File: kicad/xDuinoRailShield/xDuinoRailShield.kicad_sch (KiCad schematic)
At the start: 36 parts, among them J5 Screw_Terminal_01x02, Q2 S8050, Q3 S8550, Q4 S8050, Q5 S8550, U1 TPS5430DDA, U2 6N137, U3 EL817

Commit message: Heavy refactoring
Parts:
- removed C1, C4, C5: 10uF, Capacitor_SMD:C_1206_3216Metric, symbol Device:C
- removed C2: 10nF, Capacitor_SMD:C_0805_2012Metric, symbol Device:C
- removed C3: 10uF, Capacitor_SMD:CP_Elec_6.3x3.9, symbol Device:C_Polarized
- removed C6: 1nF, Capacitor_SMD:C_0805_2012Metric, symbol Device:C
- removed D2, D6, D7, D8: D, Diode_SMD:D_SMA, symbol Device:D
- removed D4: D_Schottky, Diode_SMD:D_SMC, symbol Device:D_Schottky
- removed D5: 1N4148W, Diode_SMD:D_SOD-123, symbol Diode:1N4148W
- removed JP_RAILCOM1: SolderJumper_2_Open, Jumper:SolderJumper-2_P1.3mm_Open_TrianglePad1.0x1.5mm, symbol Jumper:SolderJumper_2_Open
- removed L1: 22uH, Inductor_SMD:L_12x12mm_H8mm, symbol Device:L
- removed Q2, Q4: S8050, Package_TO_SOT_SMD:SOT-23, symbol Transistor_BJT:S8050
- removed Q3, Q5: S8550, Package_TO_SOT_SMD:SOT-23, symbol Transistor_BJT:S8550
- removed R10: 220R, Resistor_SMD:R_0805_2012Metric_Pad1.20x1.40mm_HandSolder, symbol Device:R
- removed R11: 5k, Resistor_SMD:R_0805_2012Metric_Pad1.20x1.40mm_HandSolder, symbol Device:R
- removed R3, R7: 10k, Resistor_SMD:R_0805_2012Metric_Pad1.20x1.40mm_HandSolder, symbol Device:R
- removed R5: 1.58k, Resistor_SMD:R_0805_2012Metric_Pad1.20x1.40mm_HandSolder, symbol Device:R
- removed R5: 22k, Resistor_SMD:R_0805_2012Metric_Pad1.20x1.40mm_HandSolder, symbol Device:R
- removed R6: 1k3, Resistor_SMD:R_0805_2012Metric_Pad1.20x1.40mm_HandSolder, symbol Device:R
- removed R8: 22, Resistor_SMD:R_0805_2012Metric_Pad1.20x1.40mm_HandSolder, symbol Device:R
- removed R9: 6k8, Resistor_SMD:R_0805_2012Metric_Pad1.20x1.40mm_HandSolder, symbol Device:R
- removed U1: TPS5430DDA, Package_SO:TI_SO-PowerPAD-8_ThermalVias, symbol Regulator_Switching:TPS5430DDA
- removed U2: 6N137, Package_DIP:DIP-8_W7.62mm, symbol Isolator:6N137
- removed U3: EL817, Package_DIP:DIP-4_W7.62mm_SMDSocket_SmallPads, symbol Isolator:EL817
- D1, D3: LCSC (none) -> C2297
- R1, R2: LCSC (none) -> C26010
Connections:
- net DCC_MM: now also A1.17 (D2); no longer A1.18 (D3)
- net RAILCOM_DATA: now also A1.18 (D3); no longer A1.17 (D2)
- no-connect marks 26 -> 24
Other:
- added sheet AC-DC buck convertor (ad-dc-buck-convertor.kicad_sch)
- added sheet Digital Signal Extraction (digital-signal-extraction.kicad_sch)
- added sheet Railcom-Feedback (railcom-feedback.kicad_sch)
- moved on the sheet: A1, D1, D3, J5, R1, R2

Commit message: Shield extracted
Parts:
- removed A1: Arduino_UNO_R3, Olis_Footprints:Arduino_UNO_R3_Double_Rows, symbol MCU_Module:Arduino_UNO_R3
- removed D1, D3: LED, LED_SMD:LED_0805_2012Metric_Pad1.15x1.40mm_HandSolder, symbol Device:LED
- removed J5: Screw_Terminal_01x02, TerminalBlock_4Ucon:TerminalBlock_4Ucon_1x02_P3.50mm_Vertical, symbol Connector:Screw_Terminal_01x02
- removed R1, R2: 3k3, Resistor_SMD:R_0805_2012Metric_Pad1.20x1.40mm_HandSolder, symbol Device:R
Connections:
- no-connect marks 24 -> 1
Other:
- added sheet IO Carrier Board (io-carrier-board.kicad_sch)

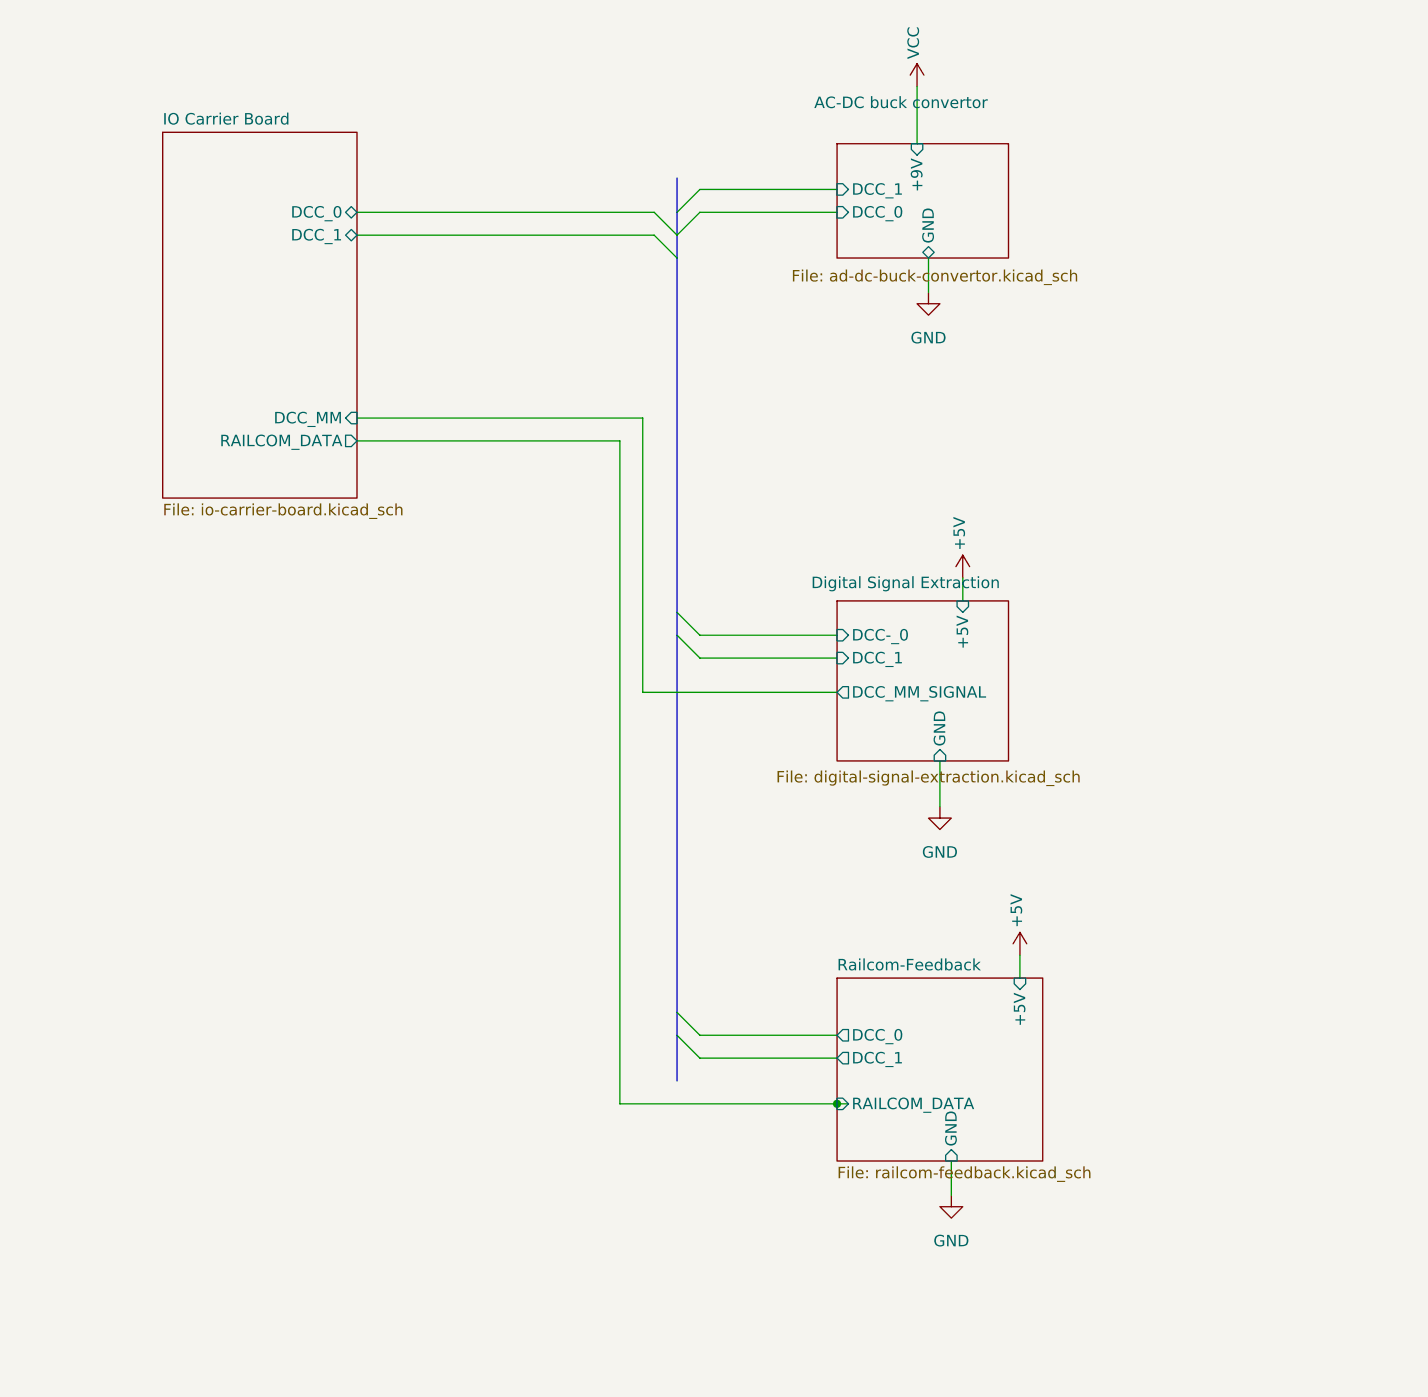
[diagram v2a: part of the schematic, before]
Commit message: Add more extractor
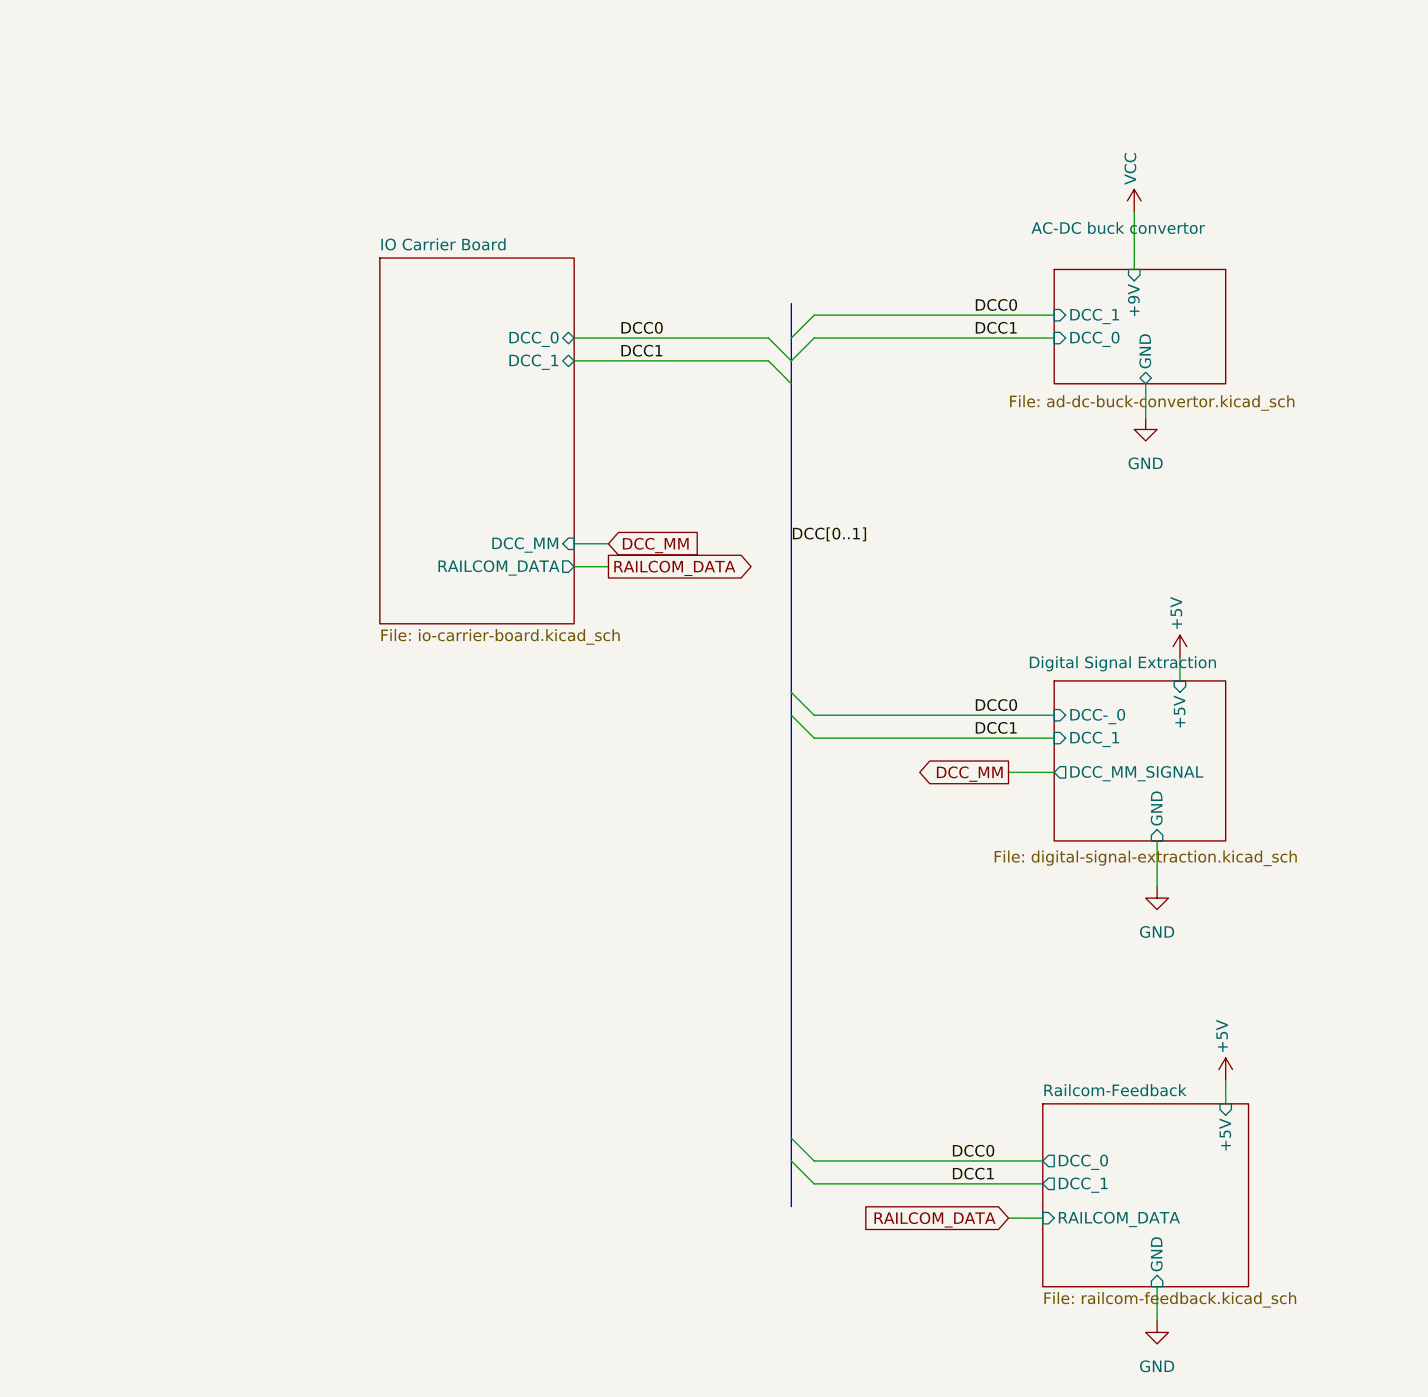
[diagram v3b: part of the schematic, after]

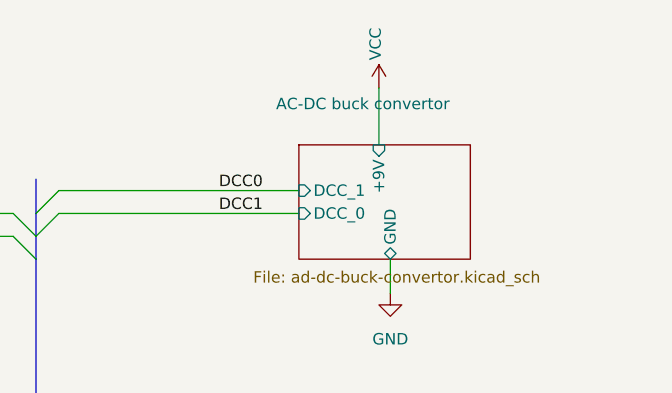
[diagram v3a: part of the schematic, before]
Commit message: More options, more Partnumbers
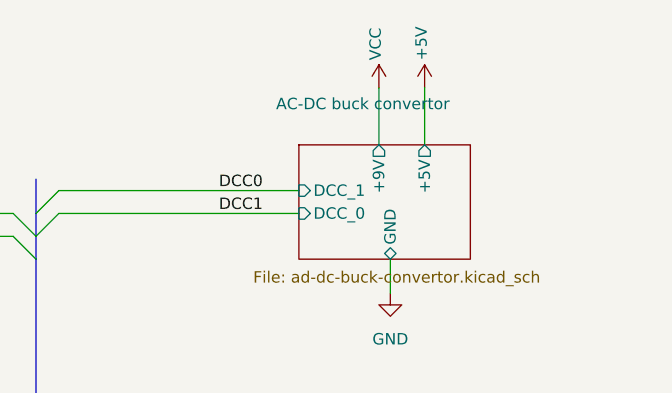
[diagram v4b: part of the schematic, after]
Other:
- sheet AC-DC buck convertor ports: added +5V; removed none
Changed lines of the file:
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@@
+    (stroke (width 0) (type default))
+  )
+  (wire (pts (xy 147.32 40.64) (xy 147.32 46.99))
     (stroke (width 0) (type default))
   )
@@
     )
   )
+  (symbol (lib_id "power:+5V") (at 147.32 40.64 0) (mirror y) (unit 1)
+    (in_bom yes) (on_board yes) (dnp no)
+    (property "Reference" "#PWR0107" (at 147.32 44.45 0)
+      (effects (font (size 1.27 1.27)) hide)
+    )
+    (property "Value" "+5V" (at 146.9644 37.592 90)
+      (effects (font (size 1.27 1.27)) (justify left))
+    )
+    (property "Footprint" "" (at 147.32 40.64 0)
+      (effects (font (size 1.27 1.27)))
+    )
+    (property "Datasheet" "" (at 147.32 40.64 0)
+      (effects (font (size 1.27 1.27)))
+    )
+    (pin "1")
+    (instances
+      (project "xDuinoRailShield"
+        (path "/e63e39d7-6ac0-4ffd-8aa3-1841a4541b55"
+          (reference "#PWR0107") (unit 1)
+        )
+      )
+    )
+  )
   (symbol (lib_id "power:VCC") (at 142.24 40.64 0) (mirror y) (unit 1)
     (in_bom yes) (on_board yes) (dnp no)
-    (property "Reference" "#PWR010" (at 142.24 44.45 0)
+    (property "Reference" "#PWR0101" (at 142.24 44.45 0)
       (effects (font (size 1.27 1.27)) hide)
     )
@@
       (project "xDuinoRailShield"
         (path "/e63e39d7-6ac0-4ffd-8aa3-1841a4541b55"
-          (reference "#PWR010") (unit 1)
+          (reference "#PWR0101") (unit 1)
         )
       )
@@
       (project "xDuinoRailShield"
         (path "/e63e39d7-6ac0-4ffd-8aa3-1841a4541b55"
-          (reference "#PWR014") (unit 1)
+          (reference "#PWR0103") (unit 1)
         )
       )
@@
       (project "xDuinoRailShield"
         (path "/e63e39d7-6ac0-4ffd-8aa3-1841a4541b55"
-          (reference "#PWR013") (unit 1)
+          (reference "#PWR0102") (unit 1)
         )
       )
@@
   (symbol (lib_id "power:+5V") (at 152.4 137.16 0) (mirror y) (unit 1)
     (in_bom yes) (on_board yes) (dnp no)
-    (property "Reference" "#PWR017" (at 152.4 140.97 0)
+    (property "Reference" "#PWR0106" (at 152.4 140.97 0)
       (effects (font (size 1.27 1.27)) hide)
     )
@@
       (project "xDuinoRailShield"
         (path "/e63e39d7-6ac0-4ffd-8aa3-1841a4541b55"
-          (reference "#PWR017") (unit 1)
+          (reference "#PWR0106") (unit 1)
         )
       )
@@
   (symbol (lib_id "power:+5V") (at 147.32 90.17 0) (mirror y) (unit 1)
     (in_bom yes) (on_board yes) (dnp no)
-    (property "Reference" "#PWR015" (at 147.32 93.98 0)
+    (property "Reference" "#PWR0105" (at 147.32 93.98 0)
       (effects (font (size 1.27 1.27)) hide)
     )
@@
       (project "xDuinoRailShield"
         (path "/e63e39d7-6ac0-4ffd-8aa3-1841a4541b55"
-          (reference "#PWR015") (unit 1)
+          (reference "#PWR0105") (unit 1)
         )
       )
@@
       (project "xDuinoRailShield"
         (path "/e63e39d7-6ac0-4ffd-8aa3-1841a4541b55"
-          (reference "#PWR016") (unit 1)
+          (reference "#PWR0104") (unit 1)
         )
       )
@@
       (effects (font (size 1.27 1.27)) (justify left))
     )
-    (pin "+9V" input (at 142.24 46.99 90)
+    (pin "+9V" output (at 142.24 46.99 90)
       (effects (font (size 1.27 1.27)) (justify right))
     )
@@
       (effects (font (size 1.27 1.27)) (justify left))
     )
-    (instances
+    (pin "+5V" output (at 147.32 46.99 90)
+      (effects (font (size 1.27 1.27)) (justify right))
+    )
+    (instances

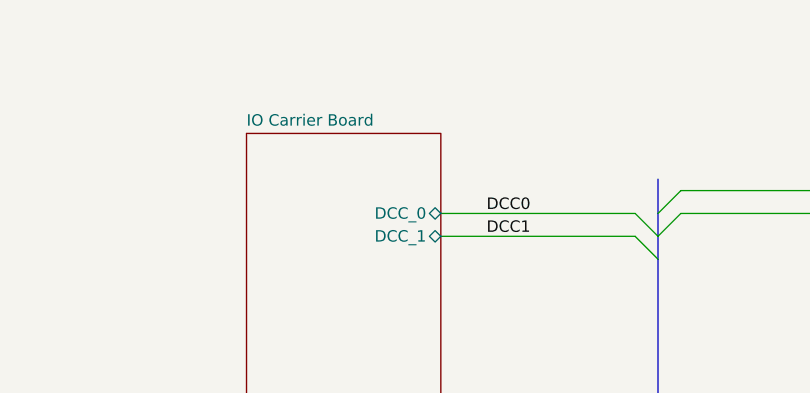
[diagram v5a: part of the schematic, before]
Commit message: Power Rails added to Arduino IO board
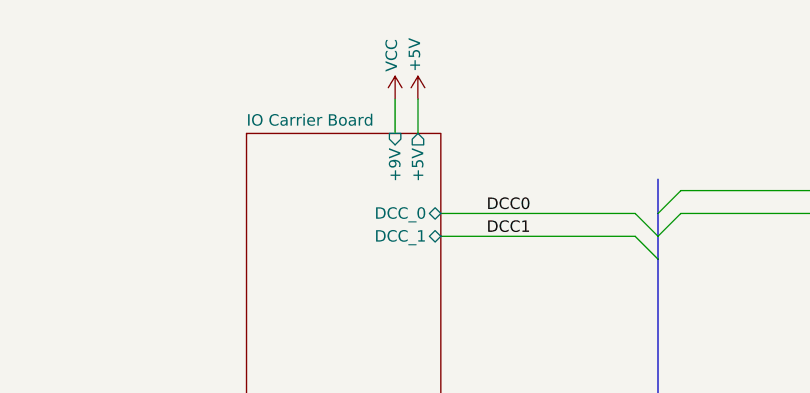
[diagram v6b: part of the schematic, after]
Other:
- sheet IO Carrier Board ports: added +5V, +9V; removed none
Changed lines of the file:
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@@
+		)
+	)
+	(wire
+		(pts
+			(xy 77.47 41.91) (xy 77.47 45.72)
+		)
+		(stroke
+			(width 0)
+			(type default)
 		)
 	)
@@
 		(pts
 			(xy 104.14 96.52) (xy 104.14 143.51)
+		)
+		(stroke
+			(width 0)
+			(type default)
+		)
+	)
+	(wire
+		(pts
+			(xy 74.93 41.91) (xy 74.93 45.72)
 		)
 		(stroke
@@
 				(justify right)
 				(hide yes)
+			)
+		)
+	)
+	(symbol
+		(lib_id "power:VCC")
+		(at 74.93 41.91 0)
+		(mirror y)
+		(unit 1)
+		(exclude_from_sim no)
+		(in_bom yes)
+		(on_board yes)
+		(dnp no)
+		(property "Reference" "#PWR01"
+			(at 74.93 45.72 0)
+			(effects
+				(font
+					(size 1.27 1.27)
+				)
+				(hide yes)
+			)
+		)
+		(property "Value" "VCC"
+			(at 74.549 38.862 90)
+			(effects
+				(font
+					(size 1.27 1.27)
+				)
+				(justify left)
+			)
+		)
+		(property "Footprint" ""
+			(at 74.93 41.91 0)
+			(effects
+				(font
+					(size 1.27 1.27)
+				)
+				(hide yes)
+			)
+		)
+		(property "Datasheet" ""
+			(at 74.93 41.91 0)
+			(effects
+				(font
+					(size 1.27 1.27)
+				)
+				(hide yes)
+			)
+		)
+		(property "Description" ""
+			(at 74.93 41.91 0)
+			(effects
+				(font
+					(size 1.27 1.27)
+				)
+				(hide yes)
+			)
+		)
+		(pin "1"
+		)
+		(instances
+			(project "xDuinoRailShield"
+				(path "/e63e39d7-6ac0-4ffd-8aa3-1841a4541b55"
+					(reference "#PWR01")
+					(unit 1)
+				)
 			)
 		)
@@
 	(symbol
 		(lib_id "power:+5V")
+		(at 77.47 41.91 0)
+		(mirror y)
+		(unit 1)
+		(exclude_from_sim no)
+		(in_bom yes)
+		(on_board yes)
+		(dnp no)
+		(property "Reference" "#PWR02"
+			(at 77.47 45.72 0)
+			(effects
+				(font
+					(size 1.27 1.27)
+				)
+				(hide yes)
+			)
+		)
+		(property "Value" "+5V"
+			(at 77.1144 38.862 90)
+			(effects
+				(font
+					(size 1.27 1.27)
+				)
+				(justify left)
+			)
+		)
+		(property "Footprint" ""
+			(at 77.47 41.91 0)
+			(effects
+				(font
+					(size 1.27 1.27)
+				)
+			)
+		)
+		(property "Datasheet" ""
+			(at 77.47 41.91 0)
+			(effects
+				(font
+					(size 1.27 1.27)
+				)
+			)
+		)
+		(property "Description" ""
+			(at 77.47 41.91 0)
+			(effects
+				(font
+					(size 1.27 1.27)
+				)
+				(hide yes)
+			)
+		)
+		(pin "1"
+		)
+		(instances
+			(project "xDuinoRailShield"
+				(path "/e63e39d7-6ac0-4ffd-8aa3-1841a4541b55"
+					(reference "#PWR02")
+					(unit 1)
+				)
+			)
+		)
+	)
+	(symbol
+		(lib_id "power:+5V")
 		(at 147.32 90.17 0)
 		(mirror y)
@@
 			(effects
 				(font
+					(size 1.27 1.27)
+				)
+				(justify right)
+			)
+		)
+		(pin "+5V" output
+			(at 77.47 45.72 90)
+			(effects
+				(font
+					(size 1.27 1.27)
+				)
+				(justify right)
+			)
+		)
+		(pin "+9V" input
+			(at 74.93 45.72 90)
+			(effects
+				(font
